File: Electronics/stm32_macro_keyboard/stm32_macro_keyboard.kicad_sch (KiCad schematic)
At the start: 13 parts, among them U1 STM32F072CBTx

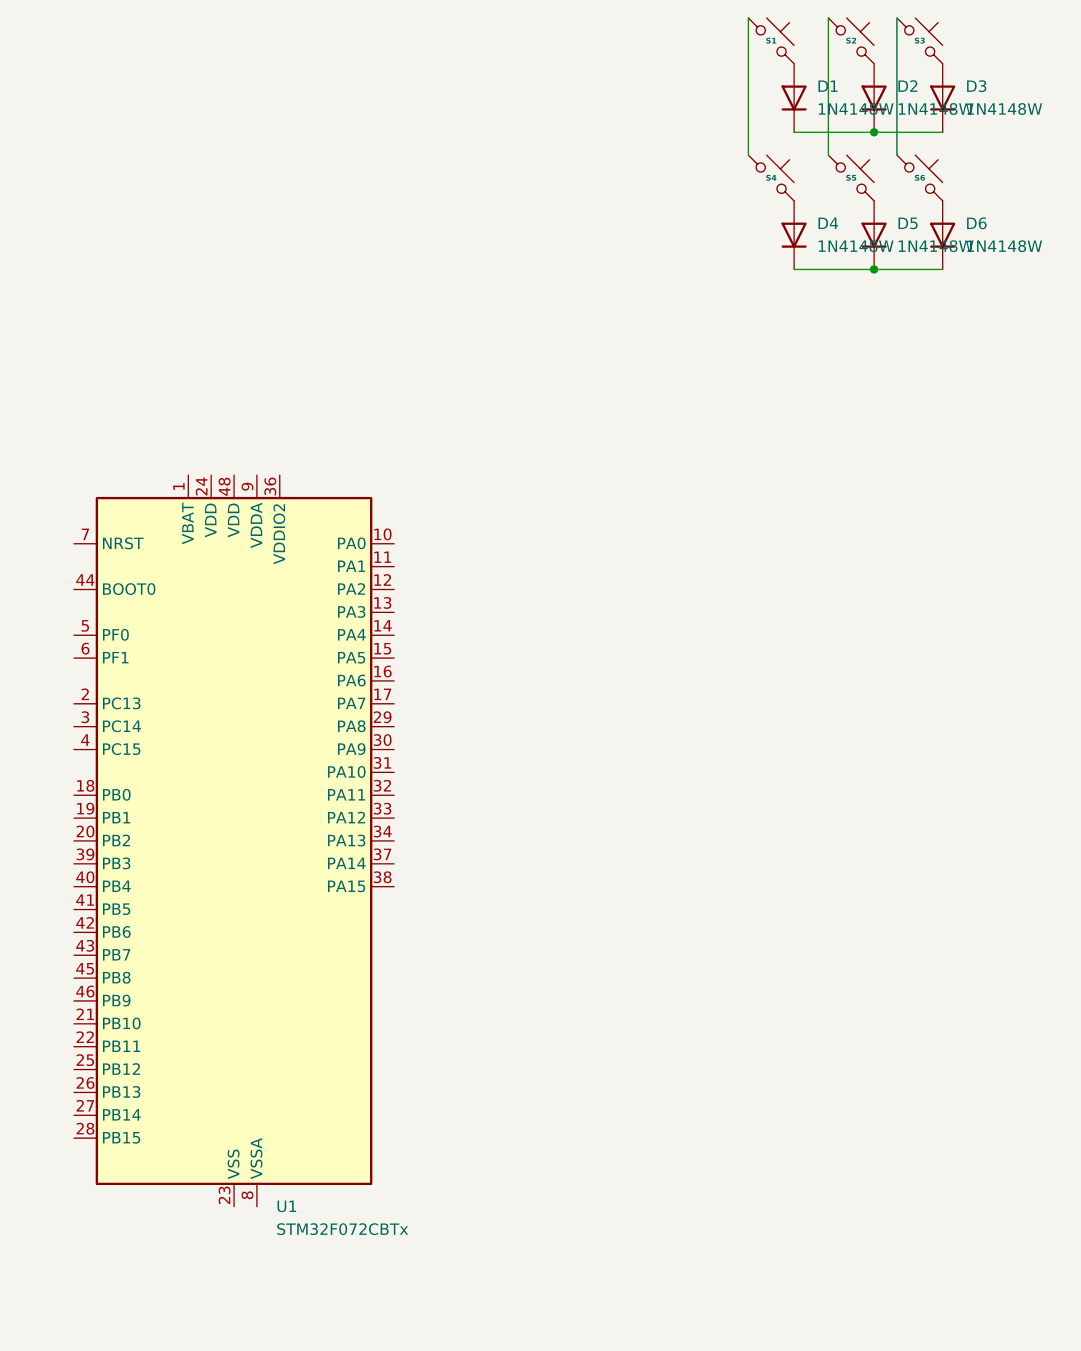
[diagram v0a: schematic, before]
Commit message: Add decoupling capacitors and BOOT0 SPDT switch for MCU power-up
- Added decoupling capacitors on VBAT, VDD, VDDA, and VSSIO2 pins
- Added SPDT switch on BOOT0 to toggle between programming and normal run mode
- Completes all circuitry required to power up the STM32 microcontroller
- Updated .gitignore to exclude KiCAD lock files and external_resources/
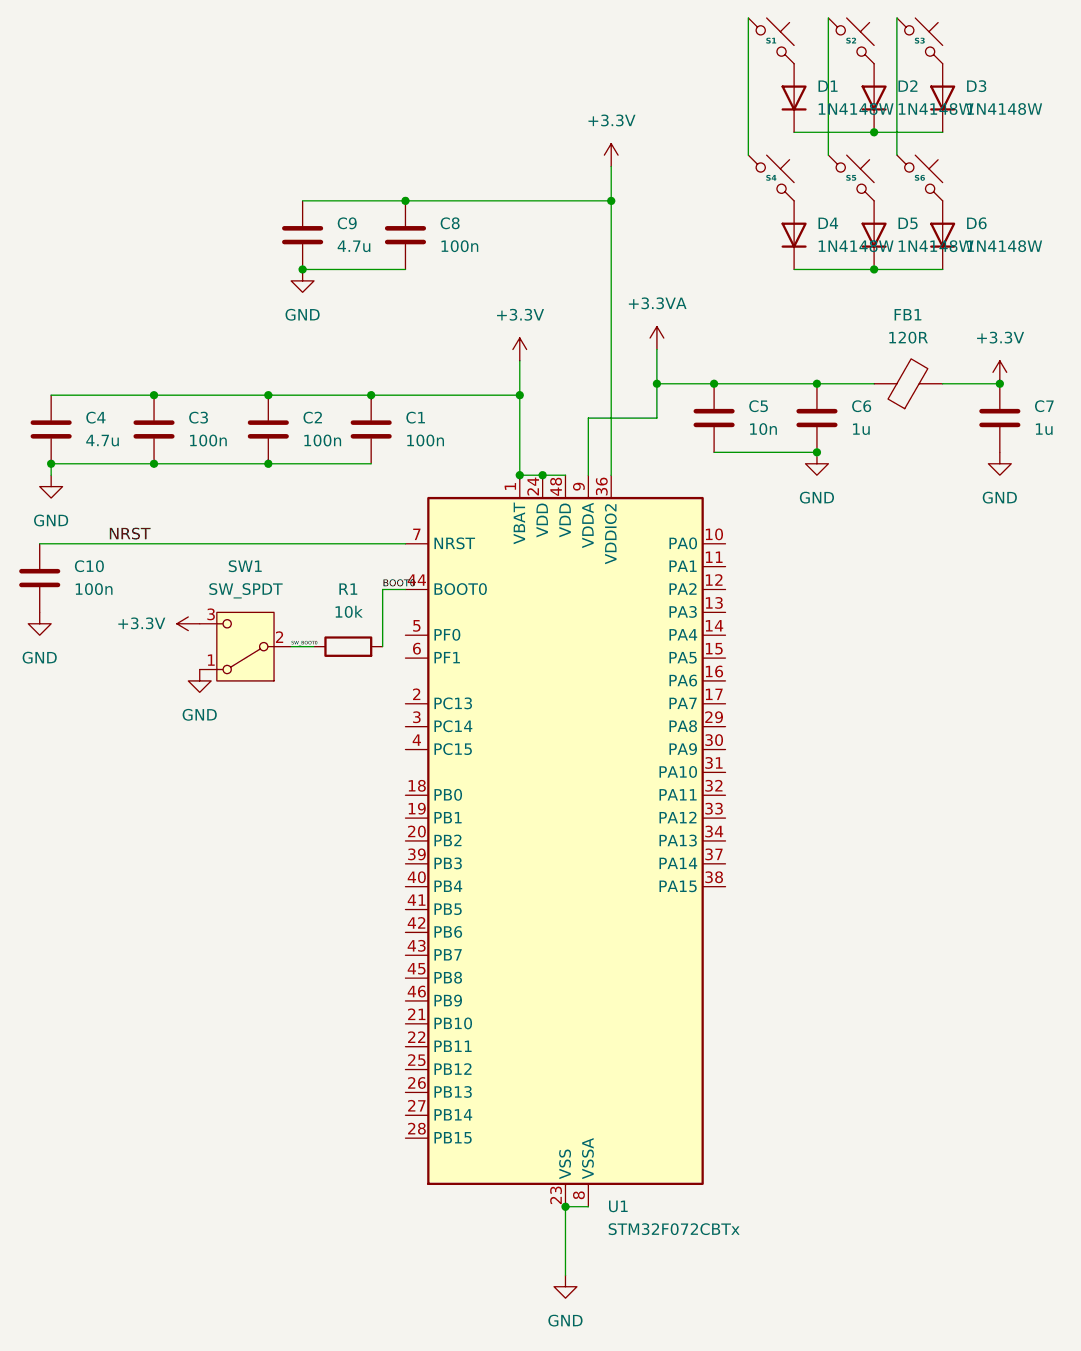
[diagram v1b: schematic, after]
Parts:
- added C1, C10, C2, C3, C8: 100n, symbol Device:C
- added C4, C9: 4.7u, symbol Device:C
- added C5: 10n, symbol Device:C
- added C6, C7: 1u, symbol Device:C
- added FB1: 120R, symbol Device:FerriteBead
- added R1: 10k, symbol Device:R
- added SW1: SW_SPDT, symbol Switch:SW_SPDT
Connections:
- net +3.3V: now reaches U1.1 (VBAT)
- net +3.3V: now also U1.24 (VDD), U1.36 (VDDIO2), U1.48 (VDD), C1.1, C2.1, C3.1, C4.1, C7.1, C8.1, C9.1, FB1.2, SW1.3 (C)
- net GND: now reaches U1.23 (VSS), U1.35 (VSS), U1.47 (VSS)
- net GND: now also U1.8 (VSSA), C1.2, C10.2, C2.2, C3.2, C4.2, C5.2, C6.2, C7.2, C8.2, C9.2, SW1.1 (A)
- net BOOT0: now reaches U1.44 (BOOT0)
- net BOOT0: now also R1.2
- net NRST: now reaches U1.7 (NRST)
- net NRST: now also C10.1
- net +3.3VA: now reaches U1.9 (VDDA)
- net +3.3VA: now also C5.1, C6.1, FB1.1
- new net SW_BOOT0: R1.1, SW1.2 (B)
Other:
- moved on the sheet: U1
